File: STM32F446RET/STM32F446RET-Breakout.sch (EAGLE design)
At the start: 30 parts, among them X1 32.768KHZ

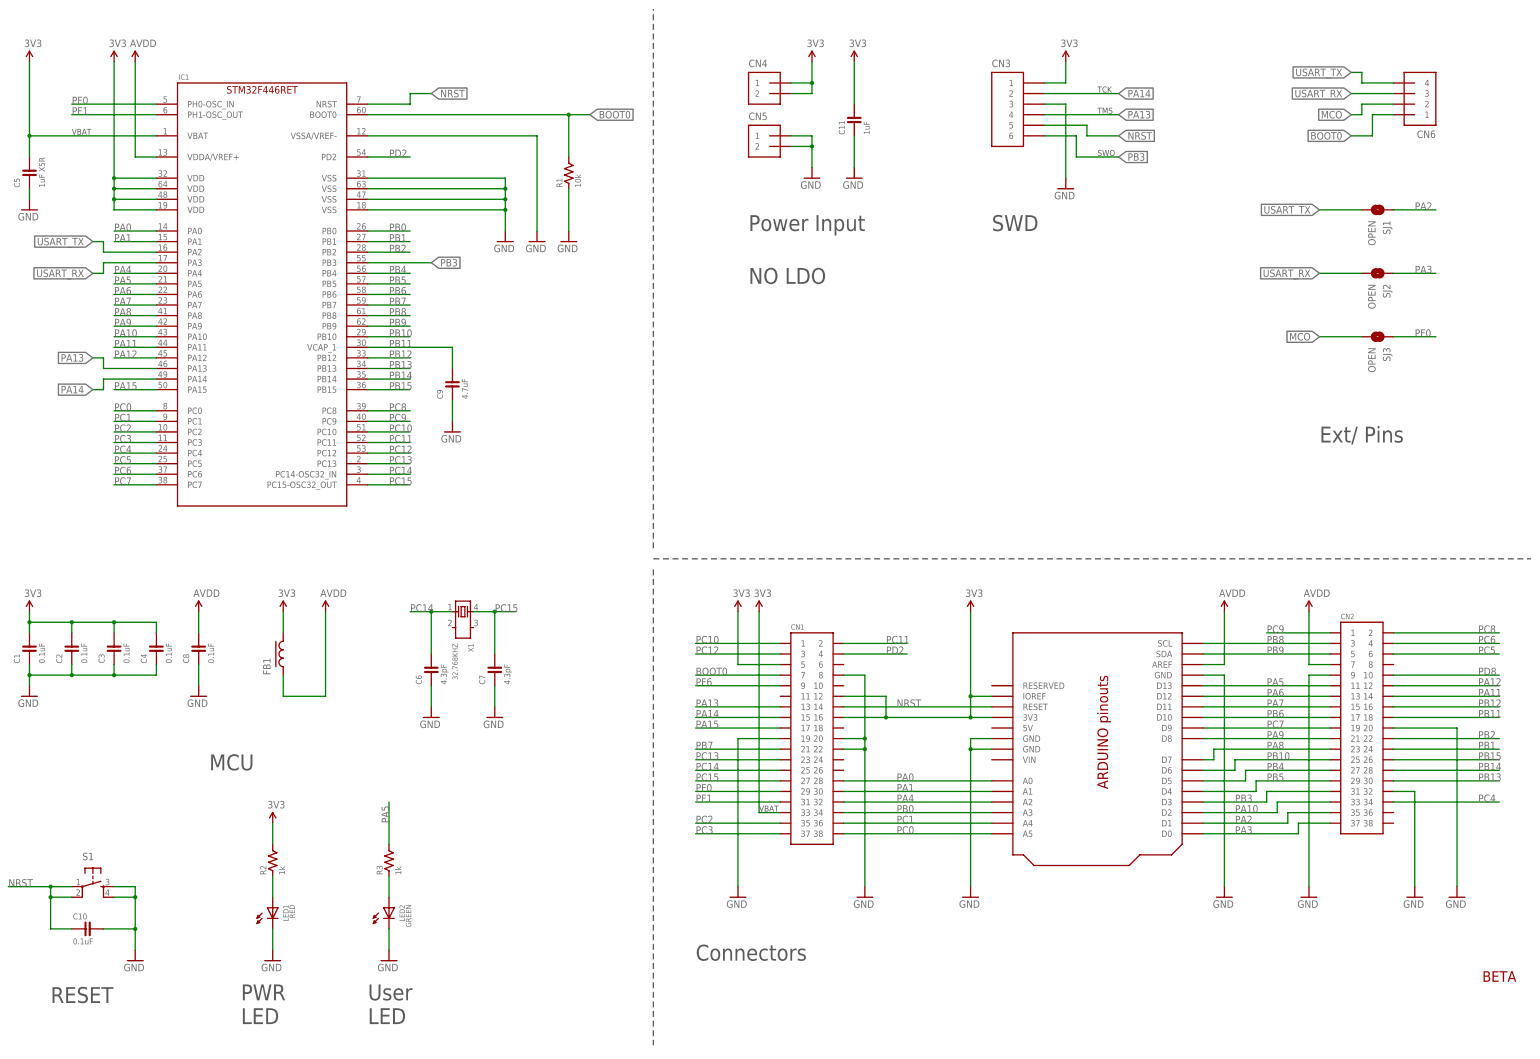
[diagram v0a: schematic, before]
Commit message: fix STM32F446RET-Breakout Rev.BETA
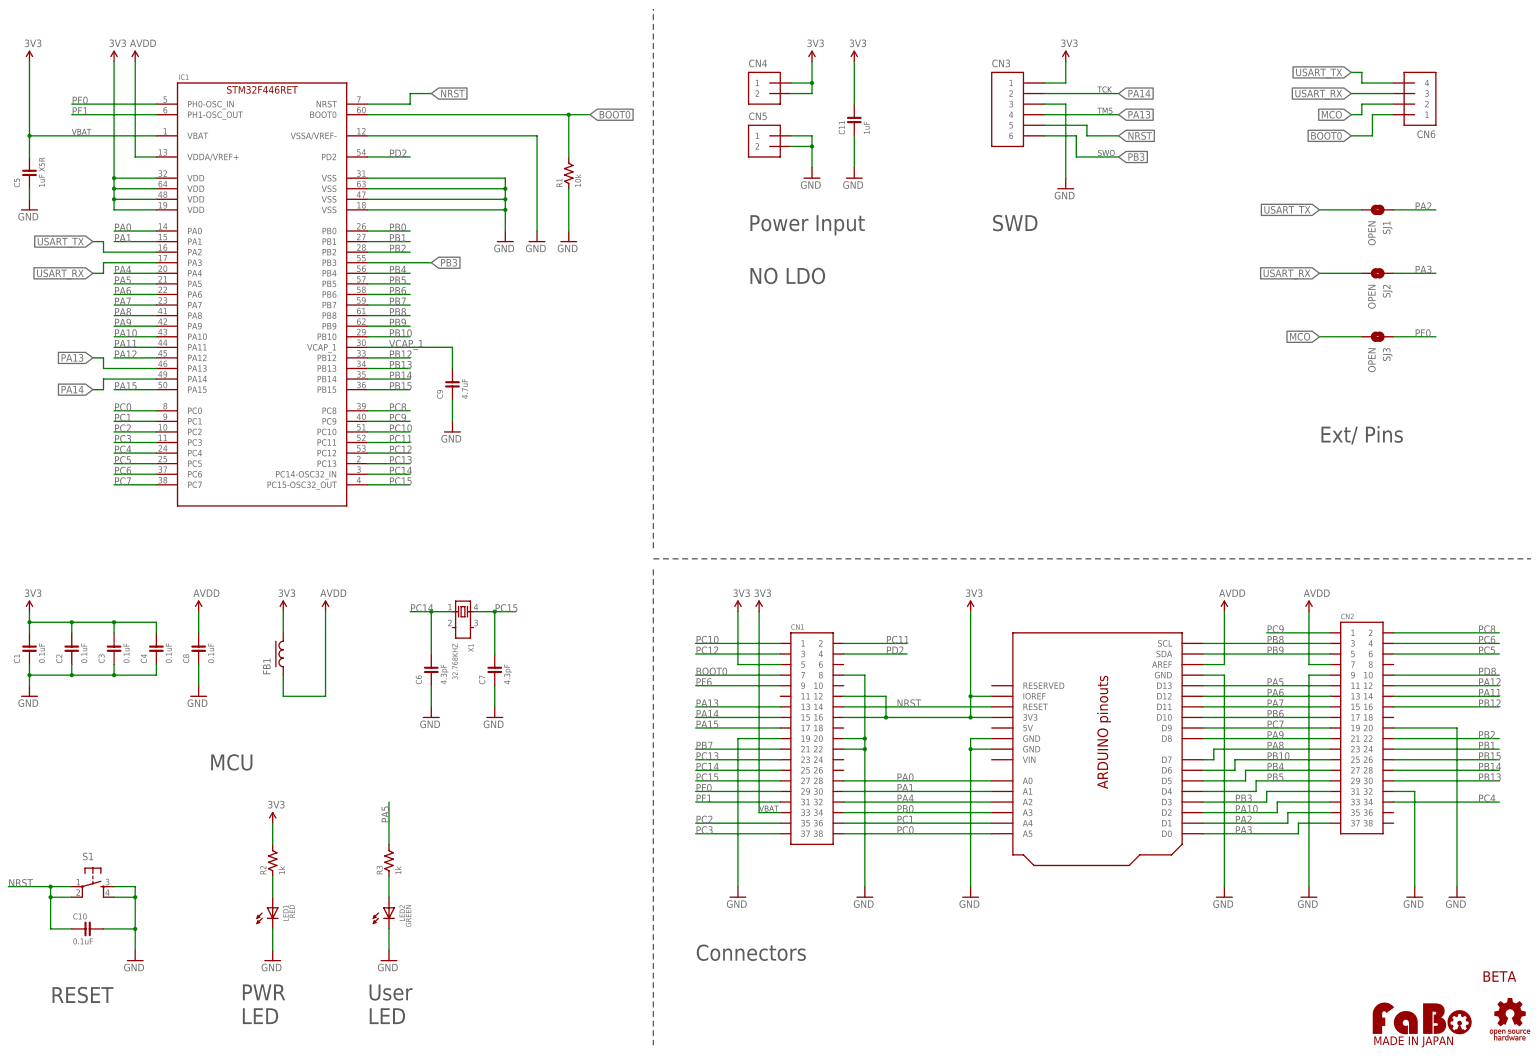
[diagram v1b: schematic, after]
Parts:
- added U$2: (no value), FaBo-etc:LOGO_FABO-M
- added U$3: (no value), FaBo-etc:LOGO_OSHW-M_BOTTOM
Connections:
- net N$1 renamed PWRLEDA
- net N$3 renamed USRLEDA
- removed net PB11: C9.2, CN2.18, IC1.VCAP_1
- new net VCAP_1: C9.2, IC1.VCAP_1
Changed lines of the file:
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@@
 <setting verticaltext="up"/>
 </settings>
-<grid distance="0.1" unitdist="inch" unit="inch" style="lines" multiple="1" display="yes" altdistance="0.01" altunitdist="inch" altunit="inch"/>
+<grid distance="0.1" unitdist="inch" unit="inch" style="lines" multiple="1" display="no" altdistance="0.01" altunitdist="inch" altunit="inch"/>
 <layers>
 <layer number="1" name="Top" color="4" fill="1" visible="no" active="no"/>
@@
 <part name="3V11" library="FaBo-Supply" deviceset="3V3" device=""/>
 <part name="GND22" library="FaBo-Supply" deviceset="GND" device=""/>
+<part name="U$2" library="FaBo-etc" deviceset="LOGO_FABO" device="-M"/>
+<part name="U$3" library="FaBo-etc" deviceset="LOGO_OSHW" device="-M_BOTTOM"/>
 </parts>
 <sheets>
@@
 <instance part="3V11" gate="G$1" x="218.44" y="241.3"/>
 <instance part="GND22" gate="G$1" x="218.44" y="215.9"/>
+<instance part="U$2" gate="G$1" x="342.9" y="5.08"/>
+<instance part="U$3" gate="G$1" x="375.92" y="12.7"/>
 </instances>
 <busses>
@@
 </segment>
 </net>
-<net name="PB11" class="0">
-<segment>
-<pinref part="CN2" gate="G$1" pin="18"/>
-<wire x1="373.38" y1="83.82" x2="347.98" y2="83.82" width="0.1524" layer="91"/>
-<label x="368.3" y="83.82" size="1.778" layer="95"/>
-</segment>
+<net name="VCAP_1" class="0">
 <segment>
 <pinref part="IC1" gate="G$1" pin="VCAP_1"/>
@@
 </segment>
 </net>
-<net name="N$1" class="0">
+<net name="PWRLEDA" class="0">
 <segment>
 <pinref part="R2" gate="G$1" pin="1"/>
@@
 </segment>
 </net>
-<net name="N$3" class="0">
+<net name="USRLEDA" class="0">
 <segment>
 <pinref part="R3" gate="G$1" pin="1"/>
